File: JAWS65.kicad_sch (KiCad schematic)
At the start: 14 parts, among them SW1 SW_Push, U1 ATmega32U4-A, Y1 16MHz

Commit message: Finished part 1
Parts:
- removed C2, C3, C4, C5: 0.1uF, symbol Device:C_Small
- removed C6, C7: 22pF, symbol Device:C_Small
- removed R2, R3: 22, symbol Device:R_Small
- removed R4: 10k, symbol Device:R_Small
- removed SW1: SW_Push, symbol Switch:SW_Push
- removed Y1: 16MHz, symbol Device:Crystal_GND24_Small
- added C? (x4): 0.1u, symbol Device:C_Small
- added C? (x2): 22p, symbol Device:C_Small
- added C?: 10u, symbol Device:C_Small
- added F?: 500m, symbol Device:Polyfuse_Small
- added J1: AVR-ISP-6, symbol Connector:AVR-ISP-6
- added R?: 10k, symbol Device:R_Small
- added R? (x2): 22, symbol Device:R_Small
- added R?: 5.1k, symbol Device:R_Small
- added R?: 5.1, symbol Device:R_Small
- added SW?: SW_Push_Reset, symbol local:SW_SKQG
- added U2: PRTR5V0U2X, symbol random-keyboard-parts:PRTR5V0U2X
- added USB1: HRO-TYPE-C-31-M-12, symbol Type-C:HRO-TYPE-C-31-M-12
- added X?: XTAL, symbol Device:Crystal_GND24_Small
- C?: renamed from C1; value 1uF -> 1u
- renumbered R1 to R?
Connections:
- net +5V: now also C?.1, C?.1, C?.1, C?.1, C?.1, F?.1, J1.2 (VCC), R?.1
- net D+: now also U1.4 (D+), R?.1
- net D-: now also U1.3 (D-), R?.2
- net GND: now also C?.2, C?.2, C?.2, C?.2, C?.2, C?.2, C?.2, J1.6 (GND), R?.1, R?.2, SW?., U2.1 (GND), USB1.1 (GND), USB1.12 (GND), USB1.13 (SHIELD), X?.2, X?.4
- net MOSI: now reaches U1.10 (PB2)
- net MOSI: now also J1.4 (MOSI)
- net MISO: now reaches U1.11 (PB3)
- net MISO: now also J1.1 (MISO)
- net RESET: now reaches U1.13 (~{RESET})
- net RESET: now also J1.5 (~{RST}), R?.2, SW?.
- net XTAL2: now reaches U1.16 (XTAL2)
- net XTAL2: now also C?.1, X?.3
- net XTAL1: now reaches U1.17 (XTAL1)
- net XTAL1: now also C?.1, X?.1
- net SCK: now reaches U1.9 (PB1)
- net SCK: now also J1.3 (SCK)
- new net: R?.2, U2.2 (IO1), USB1.6 (DP1), USB1.8 (DP2)
- new net: R?.1, USB1.10 (CC2)
- new net: R?.2, USB1.4 (CC1)
- new net: R?.1, U2.3 (IO2), USB1.5 (DN2), USB1.7 (DN1)
- new net VCC: F?.2, U2.4 (VCC), USB1.11 (VBUS), USB1.2 (VBUS)
- no-connect marks 0 -> 3
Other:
- moved on the sheet: C?, R?, U1

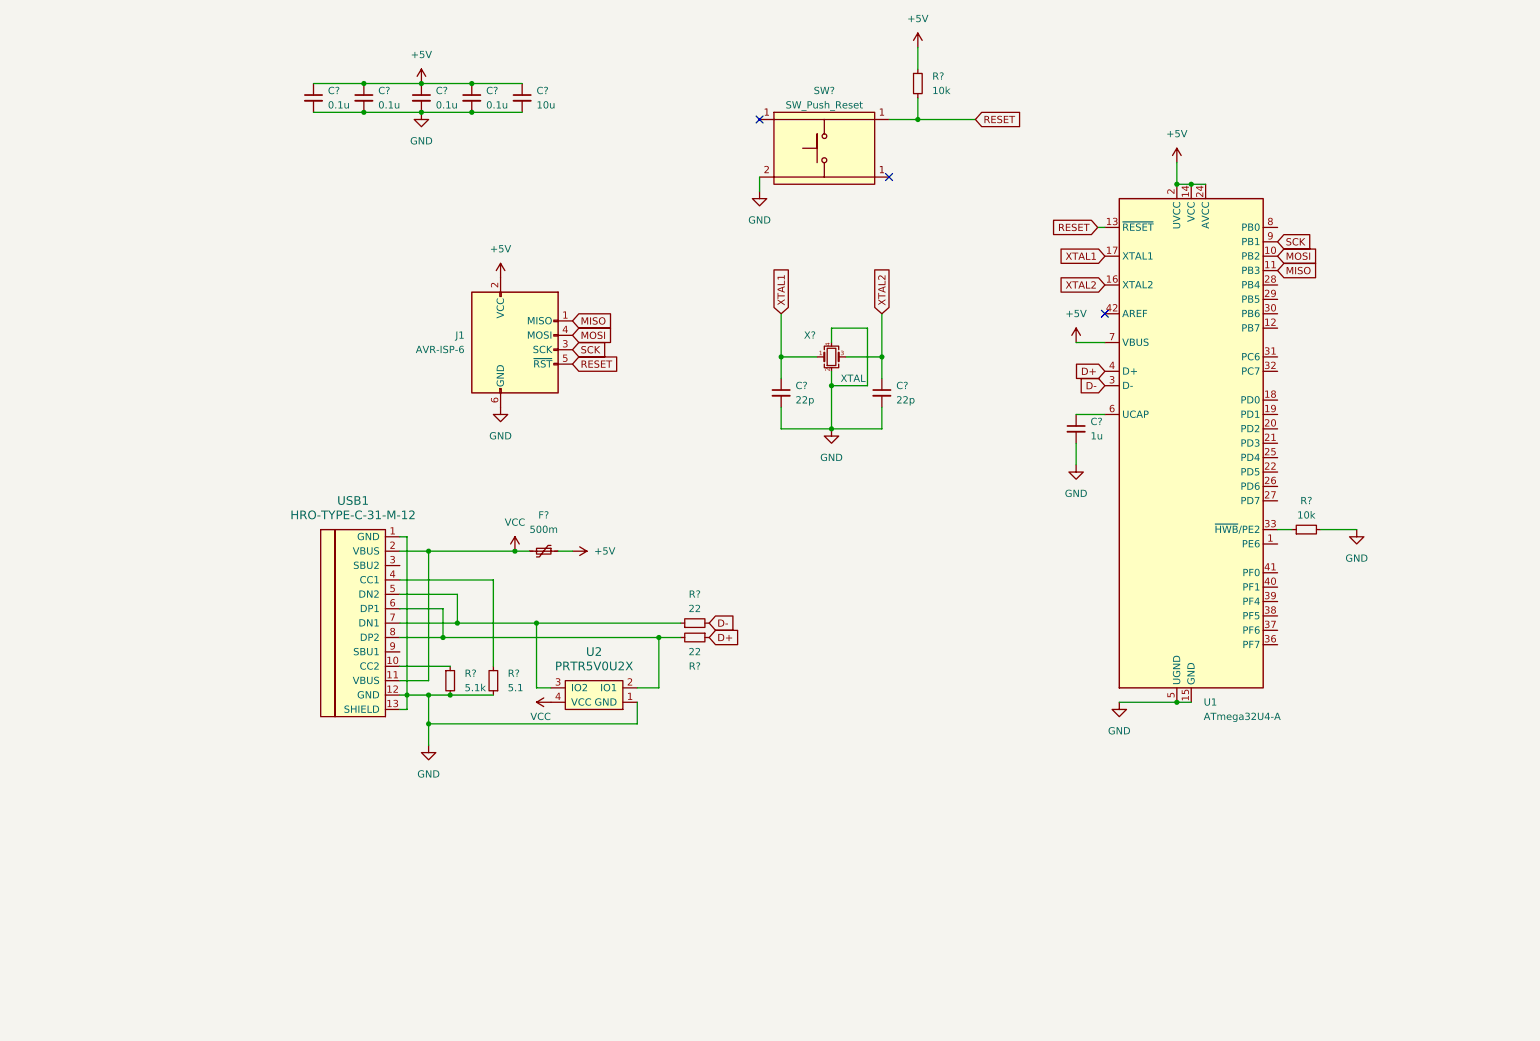
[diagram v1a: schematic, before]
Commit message: Finished Keyboard Matrix
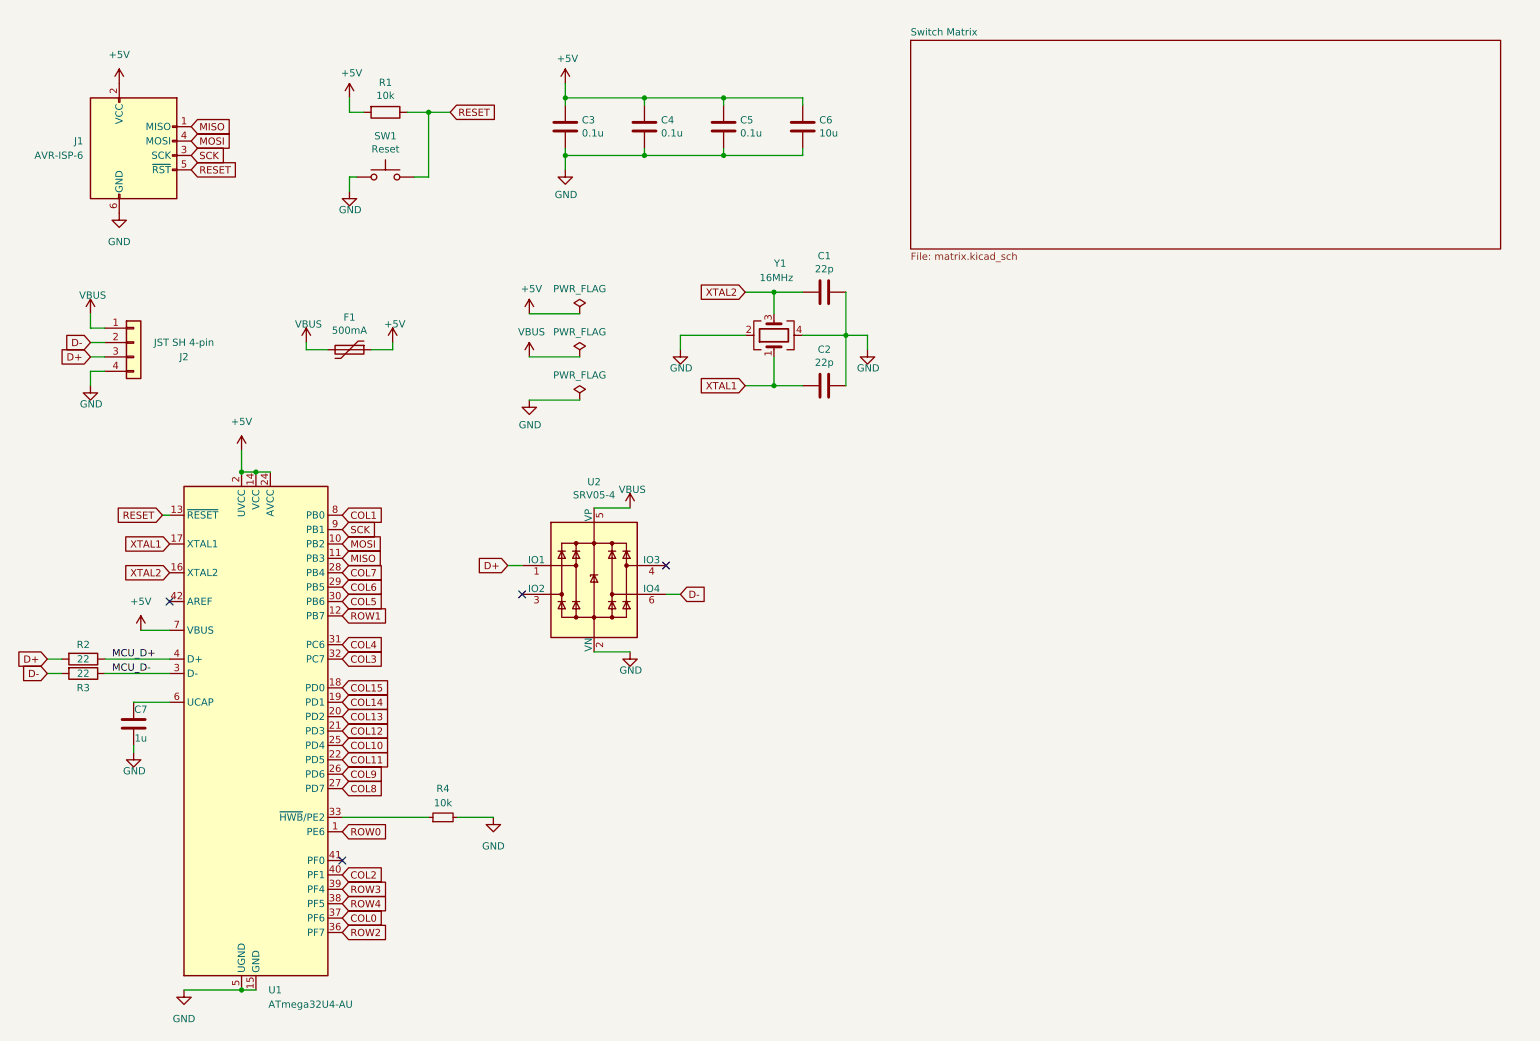
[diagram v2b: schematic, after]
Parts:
- removed C? (x4): 0.1u, symbol Device:C_Small
- removed C? (x2): 22p, symbol Device:C_Small
- removed C?: 10u, symbol Device:C_Small
- removed C?: 1u, symbol Device:C_Small
- removed F?: 500m, symbol Device:Polyfuse_Small
- removed R?: 10k, symbol Device:R_Small
- removed R? (x2): 22, symbol Device:R_Small
- removed R?: 5.1k, symbol Device:R_Small
- removed R?: 5.1, symbol Device:R_Small
- removed SW?: SW_Push_Reset, symbol local:SW_SKQG
- removed U2: PRTR5V0U2X, symbol random-keyboard-parts:PRTR5V0U2X
- removed USB1: HRO-TYPE-C-31-M-12, symbol Type-C:HRO-TYPE-C-31-M-12
- removed X?: XTAL, symbol Device:Crystal_GND24_Small
- added C1, C2: 22p, Capacitor_SMD:C_0805_2012Metric, symbol bakeneko-65-pcb-rescue:C-Device
- added C3, C4, C5: 0.1u, Capacitor_SMD:C_0805_2012Metric, symbol bakeneko-65-pcb-rescue:C-Device
- added C6: 10u, Capacitor_SMD:C_0805_2012Metric, symbol bakeneko-65-pcb-rescue:C-Device
- added C7: 1u, Capacitor_SMD:C_0805_2012Metric, symbol bakeneko-65-pcb-rescue:C-Device
- added F1: 500mA, Fuse:Fuse_1206_3216Metric, symbol bakeneko-65-pcb-rescue:Polyfuse-Device
- added J2: JST SH 4-pin, Connector_JST:JST_SH_SM04B-SRSS-TB_1x04-1MP_P1.00mm_Horizontal, symbol bakeneko-65-pcb-rescue:Conn_01x04-Connector_Generic
- added R1: 10k, Resistor_SMD:R_0805_2012Metric, symbol bakeneko-65-pcb-rescue:R-Device
- added R2, R3: 22, Resistor_SMD:R_0805_2012Metric, symbol bakeneko-65-pcb-rescue:R-Device
- added SW1: Reset, Button_Switch_SMD:SW_SPST_TL3342, symbol bakeneko-65-pcb-rescue:SW_Push-Switch
- added U2: SRV05-4, Package_TO_SOT_SMD:SOT-23-6, symbol Power_Protection:SRV05-4
- added Y1: 16MHz, Crystal:Crystal_SMD_3225-4Pin_3.2x2.5mm, symbol bakeneko-65-pcb-rescue:Crystal_GND24-Device
- J1: footprint (none) -> local:ISP
- R4: renamed from R?; footprint (none) -> Resistor_SMD:R_0805_2012Metric
- U1: value ATmega32U4-A -> ATmega32U4-AU
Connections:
- net +5V: now also C3.1, C4.1, C5.1, C6.1, F1.1, R1.2
- net D+: now also J2.3 (Pin_3), R2.2, U2.1 (IO1); no longer U1.4 (D+)
- net D-: now also J2.2 (Pin_2), R3.2, U2.6 (IO4); no longer U1.3 (D-)
- net GND: now also C1.1, C2.1, C3.2, C4.2, C5.2, C6.2, C7.2, J2.4 (Pin_4), SW1.1, U2.2 (VN), Y1.2, Y1.4
- net RESET: now also R1.1, SW1.2
- net XTAL1: now also C2.2, Y1.1
- net XTAL2: now also C1.2, Y1.3
- net ROW0: now reaches U1.1 (PE6)
- net ROW1: now reaches U1.12 (PB7)
- net COL15: now reaches U1.18 (PD0)
- net COL14: now reaches U1.19 (PD1)
- net COL13: now reaches U1.20 (PD2)
- net COL12: now reaches U1.21 (PD3)
- net COL11: now reaches U1.22 (PD5)
- net COL10: now reaches U1.25 (PD4)
- net COL9: now reaches U1.26 (PD6)
- net COL8: now reaches U1.27 (PD7)
- net COL7: now reaches U1.28 (PB4)
- net COL6: now reaches U1.29 (PB5)
- net COL5: now reaches U1.30 (PB6)
- net COL4: now reaches U1.31 (PC6)
- net COL3: now reaches U1.32 (PC7)
- net ROW2: now reaches U1.36 (PF7)
- net COL0: now reaches U1.37 (PF6)
- net ROW4: now reaches U1.38 (PF5)
- net ROW3: now reaches U1.39 (PF4)
- net COL2: now reaches U1.40 (PF1)
- net at U1.6 (UCAP): now also C7.1
- net COL1: now reaches U1.8 (PB0)
- new net MCU_D+: R2.1, U1.4 (D+)
- new net MCU_D-: R3.1, U1.3 (D-)
- new net VBUS: F1.2, J2.1 (Pin_1), U2.5 (VP)
- no-connect marks 3 -> 4
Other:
- added sheet Switch Matrix (matrix.kicad_sch)
- moved on the sheet: J1, R4, U1

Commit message: Added Hotswap + 2 MCU layouts
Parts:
- removed C7: 1u, Capacitor_SMD:C_0805_2012Metric, symbol bakeneko-65-pcb-rescue:C-Device
- removed R2, R3: 22, Resistor_SMD:R_0805_2012Metric, symbol bakeneko-65-pcb-rescue:R-Device
- removed R4: 10k, Resistor_SMD:R_0805_2012Metric, symbol Device:R_Small
- removed U1: ATmega32U4-AU, Package_QFP:TQFP-44_10x10mm_P0.8mm, symbol MCU_Microchip_ATmega:ATmega32U4-A
- added C7: 1u, Capacitor_SMD:C_0805_2012Metric, symbol mikeneko-65-pcb-rescue:C-Device
- added R2, R3: 22, Resistor_SMD:R_0805_2012Metric, symbol mikeneko-65-pcb-rescue:R-Device
- added R4: 10k, Resistor_SMD:R_0805_2012Metric, symbol mikeneko-65-pcb-rescue:R-Device
- added U2: ATmega32U4-MUR, Package_DFN_QFN:QFN-44-1EP_7x7mm_P0.5mm_EP5.2x5.2mm, symbol mikeneko-65-pcb-rescue:ATmega32U4-MU-MCU_Microchip_ATmega
- renumbered C3 to C1, C4 to C2, C5 to C3, C6 to C4, C1 to C5, C2 to C6, J2 to J1, J1 to J2, U2 to U1
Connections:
- net +5V: now also U2.14 (VCC), U2.2 (UVCC), U2.24 (AVCC), U2.34 (VCC), U2.44 (AVCC), U2.7 (VBUS)
- net COL0: now also U2.36 (PF7)
- net COL1: now also U2.37 (PF6)
- net COL10: now also U2.26 (PD6)
- net COL11: now also U2.27 (PD7)
- net COL12: now also U2.30 (PB6)
- net COL13: now also U2.29 (PB5)
- net COL14: now also U2.28 (PB4)
- net COL2: now also U2.38 (PF5)
- net COL3: now also U2.39 (PF4)
- net COL4: now also U2.40 (PF1)
- net COL5: now also U2.41 (PF0)
- net COL6: now also U2.1 (PE6)
- net COL7: now also U2.8 (PB0)
- net COL8: now also U2.12 (PB7)
- net COL9: now also U2.25 (PD4)
- net D+: now also R2.2
- net D-: now also R3.2
- net GND: now also C7.2, R4.1, U2.15 (GND), U2.23 (GND), U2.35 (GND), U2.43 (GND), U2.45 (GND), U2.5 (UGND)
- net MCU_D+: now also R2.1, U2.4 (D+)
- net MCU_D-: now also R3.1, U2.3 (D-)
- net MISO: now also U2.11 (PB3)
- net MOSI: now also U2.10 (PB2)
- net RESET: now also U2.13 (~{RESET})
- net ROW0: now also U2.18 (PD0)
- net ROW1: now also U2.19 (PD1)
- net ROW2: now also U2.20 (PD2)
- net ROW3: now also U2.21 (PD3)
- net ROW4: now also U2.32 (PC7)
- net SCK: now also U2.9 (PB1)
- net XTAL1: now also U2.17 (XTAL1)
- net XTAL2: now also U2.16 (XTAL2)
- new net: R4.2, U2.33 (~{HWB}/PE2)
- new net: C7.1, U2.6 (UCAP)
- no-connect marks 4 -> 5
